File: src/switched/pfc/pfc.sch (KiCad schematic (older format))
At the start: 67 parts, among them J1 AC-input, J2 Conn_01x02, J3 Conn_01x02, Q1 AOT190A60CL‎, U1 AP3917B, U2 bd7692fj

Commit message: footprint fix for AC input
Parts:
- J1: footprint KiCad/kicad-footprints/Connector_Wire.pretty:SolderWirePad_1x02_P7.62mm_Drill2.5mm -> custom:spacedConnector
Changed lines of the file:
@@
 Comment4 ""
 $EndDescr
-$Comp
-L Connector_Generic:Conn_01x02 J1
-U 1 1 6023F774
-P 1000 4850
-F 0 "J1" H 1080 4842 50  0000 L CNN
-F 1 "AC-input" H 1080 4751 50  0000 L CNN
-F 2 "KiCad/kicad-footprints/Connector_Wire.pretty:SolderWirePad_1x02_P7.62mm_Drill2.5mm" H 1000 4850 50  0001 C CNN
-F 3 "~" H 1000 4850 50  0001 C CNN
-F 4 "0" H 1000 4850 50  0001 C CNN "price"
-	1    1000 4850
-	-1   0    0    -1
-$EndComp
 Text GLabel 1200 4850 2    50   Input ~ 0
 v120p
@@
 Text GLabel 6900 3900 0    50   Input ~ 0
 v12
+$Comp
+L Connector_Generic:Conn_01x02 J1
+U 1 1 6023F774
+P 1000 4850
+F 0 "J1" H 1080 4842 50  0000 L CNN
+F 1 "AC-input" H 1080 4751 50  0000 L CNN
+F 2 "custom:spacedConnector" H 1000 4850 50  0001 C CNN
+F 3 "~" H 1000 4850 50  0001 C CNN
+F 4 "0" H 1000 4850 50  0001 C CNN "price"
+	1    1000 4850
+	-1   0    0    -1
+$EndComp
 $EndSCHEMATC

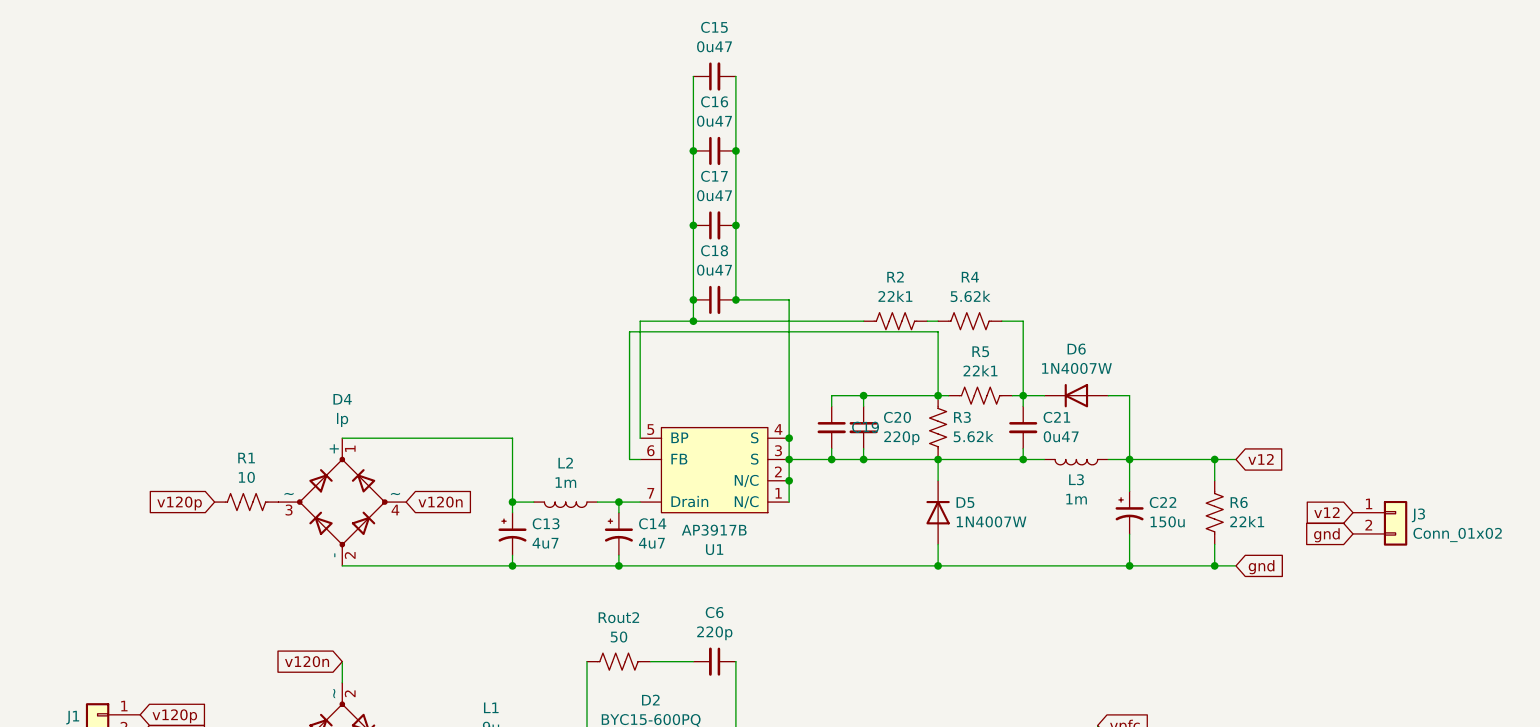
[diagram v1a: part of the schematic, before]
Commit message: pfc footprint fix
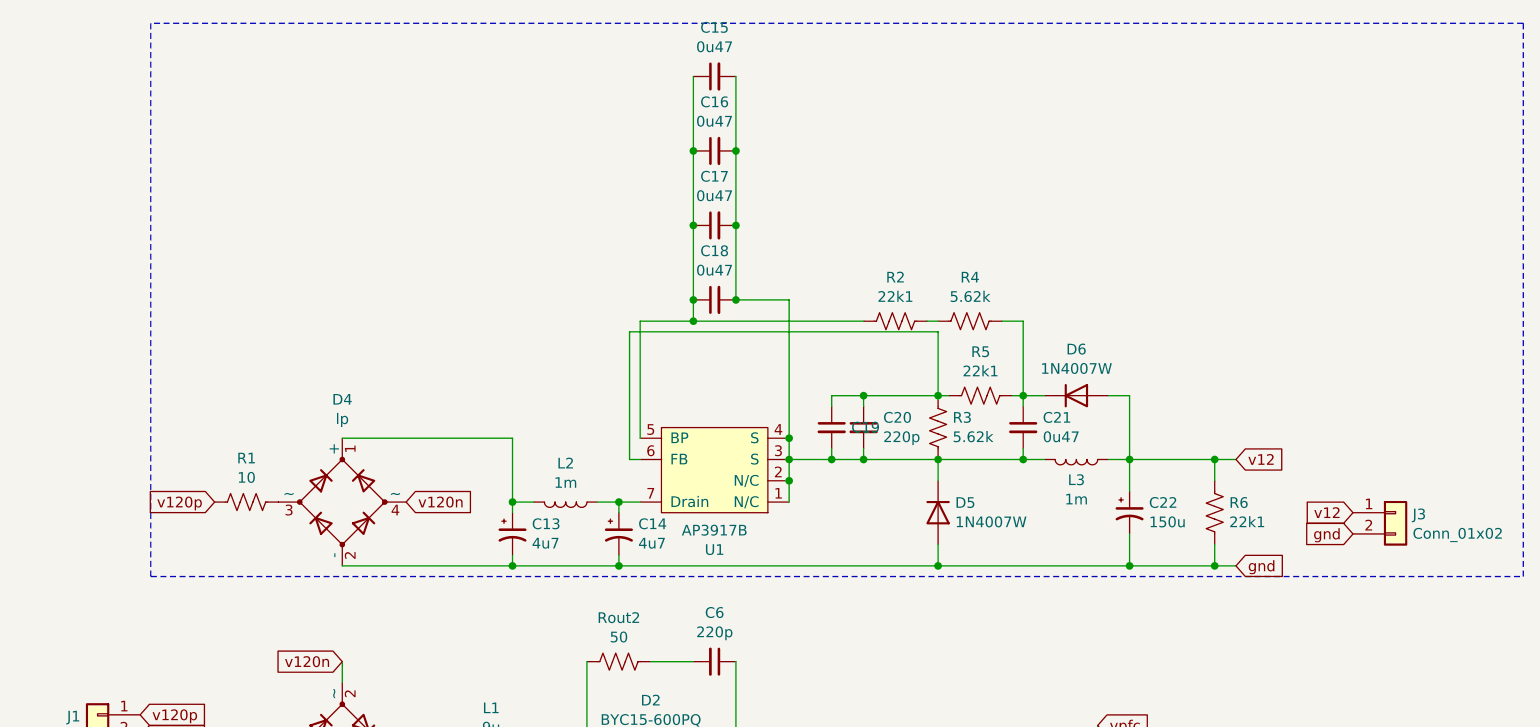
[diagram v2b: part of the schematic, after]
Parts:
- C1, C11, C2: footprint KiCad/kicad-footprints/Capacitor_SMD.pretty:C_1812_4532Metric_Pad1.30x3.40mm_HandSolder -> KiCad/Capacitors_SMD.pretty:C_1812_HandSoldering; Checked (none) -> yes; Working voltage (none) -> 500
- C19, C20, C3, C6: Checked (none) -> yes; Working voltage (none) -> 1kv
- C4: Working voltage (none) -> 35
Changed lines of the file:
@@
 F 0 "C2" H 2742 5446 50  0000 L CNN
 F 1 "470n" H 2742 5355 50  0000 L CNN
-F 2 "KiCad/kicad-footprints/Capacitor_SMD.pretty:C_1812_4532Metric_Pad1.30x3.40mm_HandSolder" H 2650 5400 50  0001 C CNN
-F 3 "~" H 2650 5400 50  0001 C CNN
+F 2 "KiCad/Capacitors_SMD.pretty:C_1812_HandSoldering" H 2650 5400 50  0001 C CNN
+F 3 "C692318" H 2650 5400 50  0001 C CNN
 F 4 "https://lcsc.com/product-detail/Multilayer-Ceramic-Capacitors-MLCC-SMD-SMT_PSA-Prosperity-Dielectrics-FM43X474K501EGG_C692318.html" H 2650 5400 50  0001 C CNN "link"
 F 5 "0.0143" H 2650 5400 50  0001 C CNN "price"
+F 6 "yes" H 2650 5400 50  0001 C CNN "Checked"
+F 7 "500" H 2650 5400 50  0001 C CNN "Working voltage"
 	1    2650 5400
 	1    0    0    -1
@@
 F 4 "https://lcsc.com/product-detail/Aluminum-Electrolytic-Capacitors-Leaded_CX-Dongguan-Chengxing-Elec-22uF-35V-5-7_C45073.html" H 3600 7100 50  0001 C CNN "link"
 F 5 "0.0125" H 3600 7100 50  0001 C CNN "price"
+F 6 "35" H 3600 7100 50  0001 C CNN "Working voltage"
 	1    3600 7100
 	1    0    0    -1
@@
 F 0 "C1" H 2392 5446 50  0000 L CNN
 F 1 "470n" H 2392 5355 50  0000 L CNN
-F 2 "KiCad/kicad-footprints/Capacitor_SMD.pretty:C_1812_4532Metric_Pad1.30x3.40mm_HandSolder" H 2300 5400 50  0001 C CNN
-F 3 "~" H 2300 5400 50  0001 C CNN
+F 2 "KiCad/Capacitors_SMD.pretty:C_1812_HandSoldering" H 2300 5400 50  0001 C CNN
+F 3 "C692318" H 2300 5400 50  0001 C CNN
 F 4 "https://lcsc.com/product-detail/Multilayer-Ceramic-Capacitors-MLCC-SMD-SMT_PSA-Prosperity-Dielectrics-FM43X474K501EGG_C692318.html" H 2300 5400 50  0001 C CNN "link"
 F 5 "0.0143" H 2300 5400 50  0001 C CNN "price"
+F 6 "yes" H 2300 5400 50  0001 C CNN "Checked"
+F 7 "500" H 2300 5400 50  0001 C CNN "Working voltage"
 	1    2300 5400
 	1    0    0    -1
@@
 F 0 "C11" H 5142 5146 50  0000 L CNN
 F 1 "470n" H 5142 5055 50  0000 L CNN
-F 2 "KiCad/kicad-footprints/Capacitor_SMD.pretty:C_1812_4532Metric_Pad1.30x3.40mm_HandSolder" H 5050 5100 50  0001 C CNN
-F 3 "~" H 5050 5100 50  0001 C CNN
+F 2 "KiCad/Capacitors_SMD.pretty:C_1812_HandSoldering" H 5050 5100 50  0001 C CNN
+F 3 "C692318" H 5050 5100 50  0001 C CNN
 F 4 "https://lcsc.com/product-detail/Multilayer-Ceramic-Capacitors-MLCC-SMD-SMT_PSA-Prosperity-Dielectrics-FM43X474K501EGG_C692318.html" H 5050 5100 50  0001 C CNN "link"
 F 5 "0.0143" H 5050 5100 50  0001 C CNN "price"
+F 6 "yes" H 5050 5100 50  0001 C CNN "Checked"
+F 7 "500" H 5050 5100 50  0001 C CNN "Working voltage"
 	1    5050 5100
 	1    0    0    -1
@@
 F 1 "220p" H 2742 5655 50  0000 L CNN
 F 2 "KiCad/kicad-footprints/Capacitor_SMD.pretty:C_1206_3216Metric_Pad1.42x1.75mm_HandSolder" H 2650 5700 50  0001 C CNN
-F 3 "~" H 2650 5700 50  0001 C CNN
+F 3 "C961523" H 2650 5700 50  0001 C CNN
 F 4 "https://lcsc.com/product-detail/Multilayer-Ceramic-Capacitors-MLCC-SMD-SMT_PSA-Prosperity-Dielectrics-FM43X474K501EGG_C692318.html" H 2650 5700 50  0001 C CNN "link"
 F 5 "0.016" H 2650 5700 50  0001 C CNN "price"
+F 6 "yes" H 2650 5700 50  0001 C CNN "Checked"
+F 7 "1kv" H 2650 5700 50  0001 C CNN "Working voltage"
 	1    2650 5700
 	1    0    0    -1
@@
 F 1 "220p" V 3762 4600 50  0000 C CNN
 F 2 "KiCad/kicad-footprints/Capacitor_SMD.pretty:C_1206_3216Metric_Pad1.42x1.75mm_HandSolder" H 3900 4600 50  0001 C CNN
-F 3 "~" H 3900 4600 50  0001 C CNN
+F 3 "C961523" H 3900 4600 50  0001 C CNN
 F 4 "https://lcsc.com/product-detail/Multilayer-Ceramic-Capacitors-MLCC-SMD-SMT_PSA-Prosperity-Dielectrics-FM43X474K501EGG_C692318.html" H 3900 4600 50  0001 C CNN "link"
 F 5 "0.016" H 3900 4600 50  0001 C CNN "price"
+F 6 "yes" H 3900 4600 50  0001 C CNN "Checked"
+F 7 "1kv" H 3900 4600 50  0001 C CNN "Working voltage"
 	1    3900 4600
 	0    1    1    0
@@
 F 1 "220p" H 4692 3455 50  0000 L CNN
 F 2 "KiCad/kicad-footprints/Capacitor_SMD.pretty:C_1206_3216Metric_Pad1.42x1.75mm_HandSolder" H 4600 3500 50  0001 C CNN
-F 3 "~" H 4600 3500 50  0001 C CNN
+F 3 "C961523" H 4600 3500 50  0001 C CNN
 F 4 "https://lcsc.com/product-detail/Multilayer-Ceramic-Capacitors-MLCC-SMD-SMT_PSA-Prosperity-Dielectrics-FM43X474K501EGG_C692318.html" H 4600 3500 50  0001 C CNN "link"
 F 5 "0.016" H 4600 3500 50  0001 C CNN "price"
+F 6 "yes" H 4600 3500 50  0001 C CNN "Checked"
+F 7 "1kv" H 4600 3500 50  0001 C CNN "Working voltage"
 	1    4600 3500
 	1    0    0    -1
@@
 F 1 "220p" H 4542 3455 50  0001 L CNN
 F 2 "KiCad/kicad-footprints/Capacitor_SMD.pretty:C_1206_3216Metric_Pad1.42x1.75mm_HandSolder" H 4450 3500 50  0001 C CNN
-F 3 "~" H 4450 3500 50  0001 C CNN
+F 3 "C961523" H 4450 3500 50  0001 C CNN
 F 4 "https://lcsc.com/product-detail/Multilayer-Ceramic-Capacitors-MLCC-SMD-SMT_PSA-Prosperity-Dielectrics-FM43X474K501EGG_C692318.html" H 4450 3500 50  0001 C CNN "link"
 F 5 "0.016" H 4450 3500 50  0001 C CNN "price"
+F 6 "yes" H 4450 3500 50  0001 C CNN "Checked"
+F 7 "1kv" H 4450 3500 50  0001 C CNN "Working voltage"
 	1    4450 3500
 	1    0    0    -1
@@
 	-1   0    0    -1
 $EndComp
+Wire Notes Line
+	7700 4200 7700 1600
+Wire Notes Line
+	7700 1600 1250 1600
+Wire Notes Line
+	1250 1600 1250 4200
+Wire Notes Line
+	1250 4200 7700 4200
 $EndSCHEMATC

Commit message: fixing footprint references
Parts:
- C1, C11, C2: footprint KiCad/Capacitors_SMD.pretty:C_1812_HandSoldering -> Capacitor_SMD:C_1812_4532Metric_Pad1.57x3.40mm_HandSolder
- C10, C5, C7, C9: footprint KiCad/kicad-footprints/Capacitor_THT.pretty:CP_Radial_D16.0mm_P7.50mm -> Capacitor_THT:CP_Radial_D16.0mm_P7.50mm
- C12, C15, C16, C17, C18, C21, C8, Ceo1, Ceo2, Cisf1: footprint KiCad/kicad-footprints/Capacitor_SMD.pretty:C_0603_1608Metric_Pad1.05x0.95mm_HandSolder -> Capacitor_SMD:C_0603_1608Metric_Pad1.08x0.95mm_HandSolder
- C13, C14: footprint KiCad/kicad-footprints/Capacitor_THT.pretty:CP_Radial_D8.0mm_P3.50mm -> Capacitor_THT:CP_Radial_D8.0mm_P3.50mm
- C19, C20, C3, C6: footprint KiCad/kicad-footprints/Capacitor_SMD.pretty:C_1206_3216Metric_Pad1.42x1.75mm_HandSolder -> Capacitor_SMD:C_1206_3216Metric_Pad1.33x1.80mm_HandSolder
- C22: footprint KiCad/kicad-footprints/Capacitor_THT.pretty:CP_Radial_D6.3mm_P2.50mm -> Capacitor_THT:CP_Radial_D6.3mm_P2.50mm
- C4: footprint KiCad/kicad-footprints/Capacitor_THT.pretty:CP_Radial_D5.0mm_P2.00mm -> Capacitor_THT:CP_Radial_D5.0mm_P2.00mm
- D2: footprint KiCad/kicad-footprints/Package_TO_SOT_THT.pretty:TO-220-2_Horizontal_TabDown -> Package_TO_SOT_THT:TO-220-2_Horizontal_TabDown
- D3, D5, D6: footprint KiCad/kicad-footprints/Diode_SMD.pretty:D_SOD-123F -> Diode_SMD:D_SOD-123F
- D4: footprint KiCad/kicad-footprints/Diode_SMD.pretty:Diode_Bridge_Diotec_ABS -> Diode_SMD:Diode_Bridge_Diotec_ABS
- J2: footprint KiCad/kicad-footprints/Connector_Wire.pretty:SolderWirePad_1x02_P7.62mm_Drill2.5mm -> Connector_Wire:SolderWire-2sqmm_1x02_P7.8mm_D2mm_OD3.9mm
- J3: footprint KiCad/kicad-footprints/Connector_PinHeader_2.54mm.pretty:PinHeader_1x02_P2.54mm_Vertical -> Connector_PinSocket_2.54mm:PinSocket_1x02_P2.54mm_Vertical
- L2, L3: footprint KiCad/kicad-footprints/Inductor_SMD.pretty:L_Bourns-SRN6028 -> Inductor_SMD:L_Bourns-SRN6028
- Q1: footprint KiCad/kicad-footprints/Package_TO_SOT_THT.pretty:TO-220-3_Horizontal_TabDown -> Package_TO_SOT_THT:TO-220-2_Horizontal_TabDown
- R1: footprint KiCad/kicad-footprints/Resistor_THT.pretty:R_Axial_DIN0516_L15.5mm_D5.0mm_P20.32mm_Horizontal -> Resistor_THT:R_Axial_DIN0516_L15.5mm_D5.0mm_P20.32mm_Horizontal
- R2, R3, R4, R5, R6: footprint KiCad/kicad-footprints/Resistor_THT.pretty:R_Axial_DIN0309_L9.0mm_D3.2mm_P2.54mm_Vertical -> Resistor_THT:R_Axial_DIN0309_L9.0mm_D3.2mm_P2.54mm_Vertical
- R7, R8: footprint KiCad/kicad-footprints/Resistor_THT.pretty:R_Axial_DIN0617_L17.0mm_D6.0mm_P25.40mm_Horizontal -> Resistor_THT:R_Axial_DIN0617_L17.0mm_D6.0mm_P25.40mm_Horizontal
- Reo1, Rgs1, Rout3, Rovpl1, Rt1, Rvsl1, Rvsl2: footprint KiCad/kicad-footprints/Resistor_SMD.pretty:R_0603_1608Metric_Pad1.05x0.95mm_HandSolder -> Resistor_SMD:R_0603_1608Metric_Pad0.98x0.95mm_HandSolder
- Ris1, Ris2, Ris3: footprint KiCad/kicad-footprints/Capacitor_SMD.pretty:C_2512_6332Metric_Pad1.52x3.35mm_HandSolder -> Resistor_SMD:R_2512_6332Metric_Pad1.40x3.35mm_HandSolder
- Risf1, Risf2, Route1: footprint KiCad/kicad-footprints/Resistor_THT.pretty:R_Axial_DIN0207_L6.3mm_D2.5mm_P2.54mm_Vertical -> Resistor_THT:R_Axial_DIN0207_L6.3mm_D2.5mm_P2.54mm_Vertical
- Rout1, Rout2: footprint KiCad/kicad-footprints/Resistor_THT.pretty:R_Axial_DIN0207_L6.3mm_D2.5mm_P10.16mm_Horizontal -> Resistor_SMD:R_1206_3216Metric_Pad1.30x1.75mm_HandSolder
- Rovph1, Rovph2, Rvsh1, Rvsh2: footprint KiCad/kicad-footprints/Resistor_SMD.pretty:R_1206_3216Metric_Pad1.42x1.75mm_HandSolder -> Resistor_SMD:R_1206_3216Metric_Pad1.30x1.75mm_HandSolder
- U2: footprint KiCad/kicad-footprints/Package_SO.pretty:SOP-8_6.62x9.15mm_P2.54mm -> Package_SO:SOP-8_6.62x9.15mm_P2.54mm
